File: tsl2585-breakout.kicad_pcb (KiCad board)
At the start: 2 copper layers, 25 x 18.5 mm, 13 parts, among them J1 Conn_01x08, U1 TSL2585, U2 MIC5365-1.8YC5

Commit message: Breakout board ready for fab
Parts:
- J1: moved to B.Cu
- turned J1 to -90 degrees
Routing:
- net GND: track 7.61 -> 10.7 mm, vias 3 -> 4
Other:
- board text added: "1V8"
- board text added: "GND"
- board text added: "INT"
- board text added: "SCL"
- board text added: "SDA"
- board text added: "Sensor Breakout"
- board text added: "TSL2520 TSL2521 TSL2585 TCS3410"
- board text added: "VIN"
- board text added: "VSYNC"
- board text added: "V_{PU}"

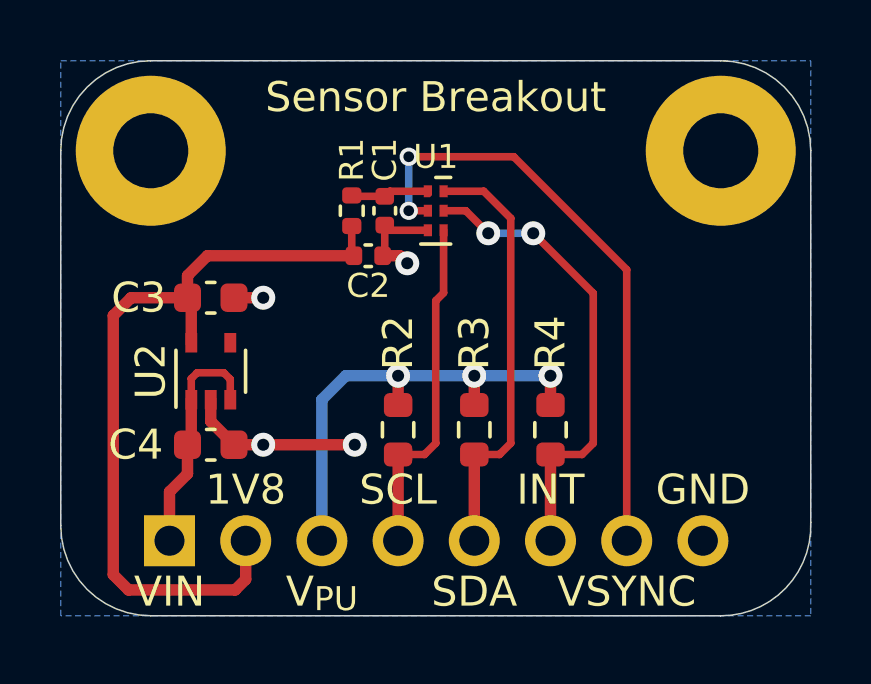
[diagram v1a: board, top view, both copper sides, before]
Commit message: Update project to remove alternative sensors
As it turns out, these other sensors are not pin compatible.
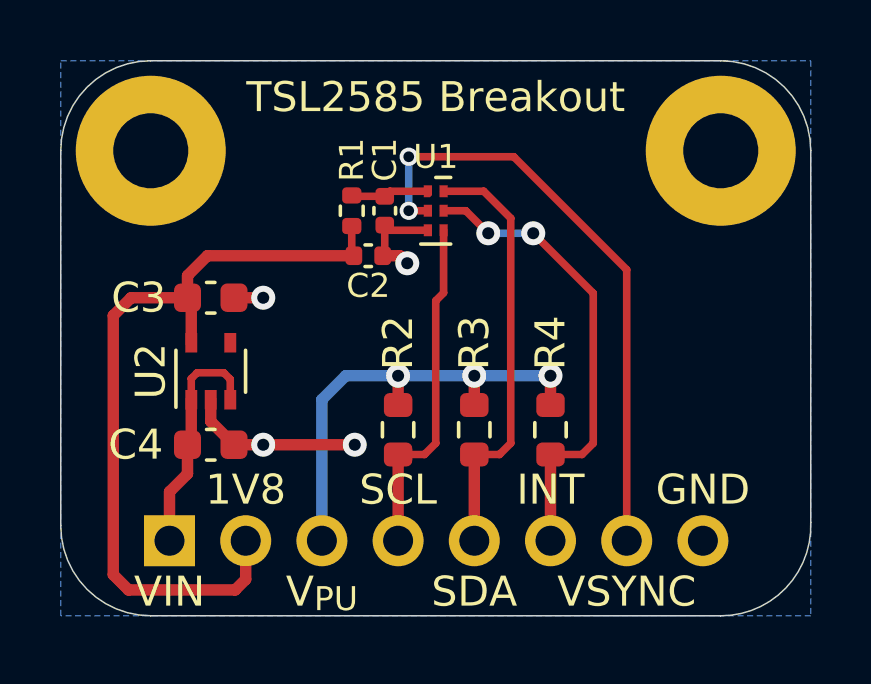
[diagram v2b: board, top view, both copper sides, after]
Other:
- board text added: "TSL2585 Breakout"
- board text removed: "Sensor Breakout"
- board text removed: "TSL2520 TSL2521 TSL2585 TCS3410"
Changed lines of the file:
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@@
     )
   )
-  (gr_rect (start 53.5 32.3) (end 54.5 31.3)
-    (stroke (width 0.12) (type solid)) (fill solid) (layer "B.SilkS"))
-  (gr_rect (start 53.5 30.7) (end 54.5 29.7)
-    (stroke (width 0.12) (type solid)) (fill solid) (layer "B.SilkS"))
-  (gr_rect (start 53.5 35.5) (end 54.5 34.5)
-    (stroke (width 0.12) (type solid)) (fill solid) (layer "B.SilkS"))
-  (gr_rect (start 53.5 33.9) (end 54.5 32.9)
-    (stroke (width 0.12) (type solid)) (fill solid) (layer "B.SilkS"))
   (gr_line (start 42.5 23) (end 42.5 41)
     (stroke (width 0.05) (type default)) (layer "Cmts.User"))
@@
   (gr_line (start 55 26) (end 55 38.37868)
     (stroke (width 0.05) (type default)) (layer "Edge.Cuts"))
-  (gr_text "TSL2520\nTSL2521\nTSL2585\nTCS3410" (at 53.2 35.7) (layer "B.SilkS")
-    (effects (font (size 1 1) (thickness 0.15)) (justify left bottom mirror))
-  )
-  (gr_text "Sensor Breakout" (at 42.5 24.8) (layer "F.SilkS")
+  (gr_text "TSL2585 Breakout" (at 42.5 24.8) (layer "F.SilkS")
     (effects (font (size 1 1) (thickness 0.15)) (justify bottom))
   )
@@
     )
   )
-  (group "" (id 86eee78b-b9e9-43e6-ac21-624bcd37a39e)
-    (members
-      32a64b0f-d6b0-4789-9c33-70a0a10073d8
-      5463b71c-086f-4dd3-b3d0-8d389406444f
-      6b5ae48a-f7e6-4fdb-95c4-cca5dc8ec693
-      9db497a7-e0ff-44ae-b4d9-30eeedc5e270
-      c9a40c2c-4713-4e21-a011-a058c0a1b2f8
-    )
-  )
